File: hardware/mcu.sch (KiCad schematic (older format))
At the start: 43 parts, among them P2 CONN_02X05, SW2 SW_PUSH, U11 TM4C1294KCPDT, Y1 NX5032GA

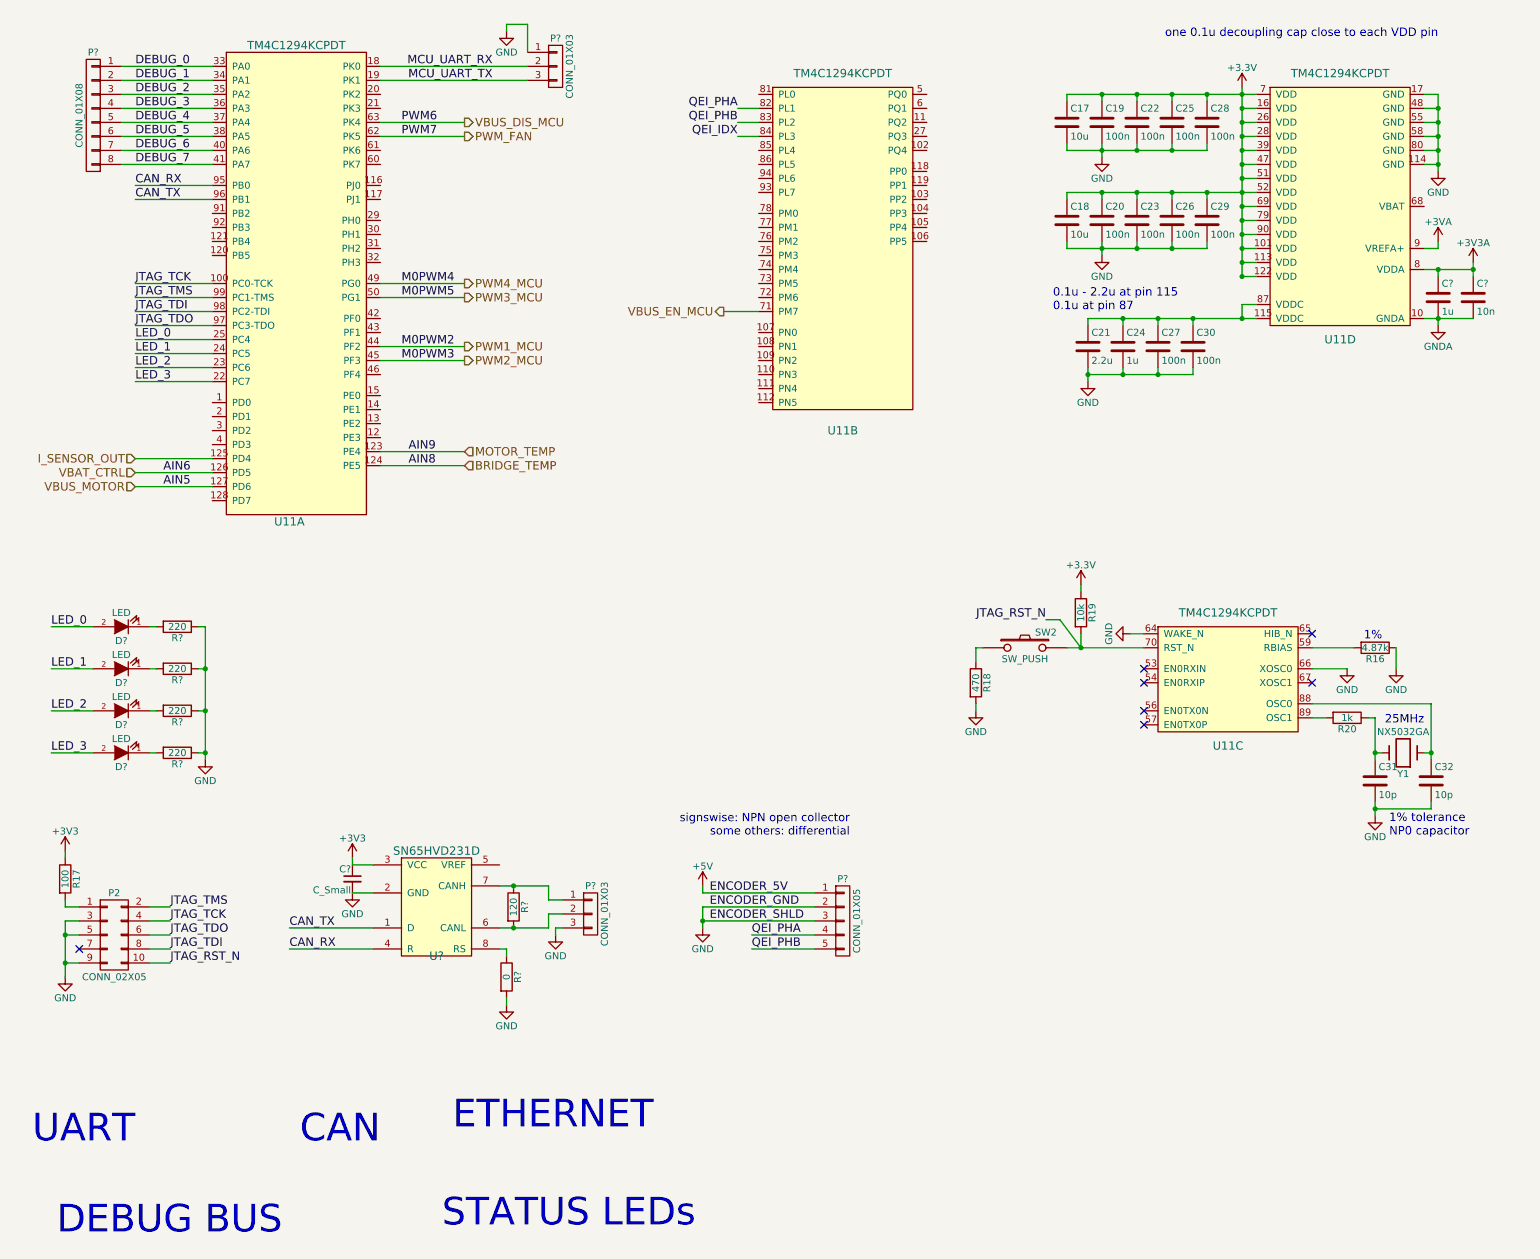
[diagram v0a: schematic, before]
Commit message: Update sensors, hbridge caps, add heatsink
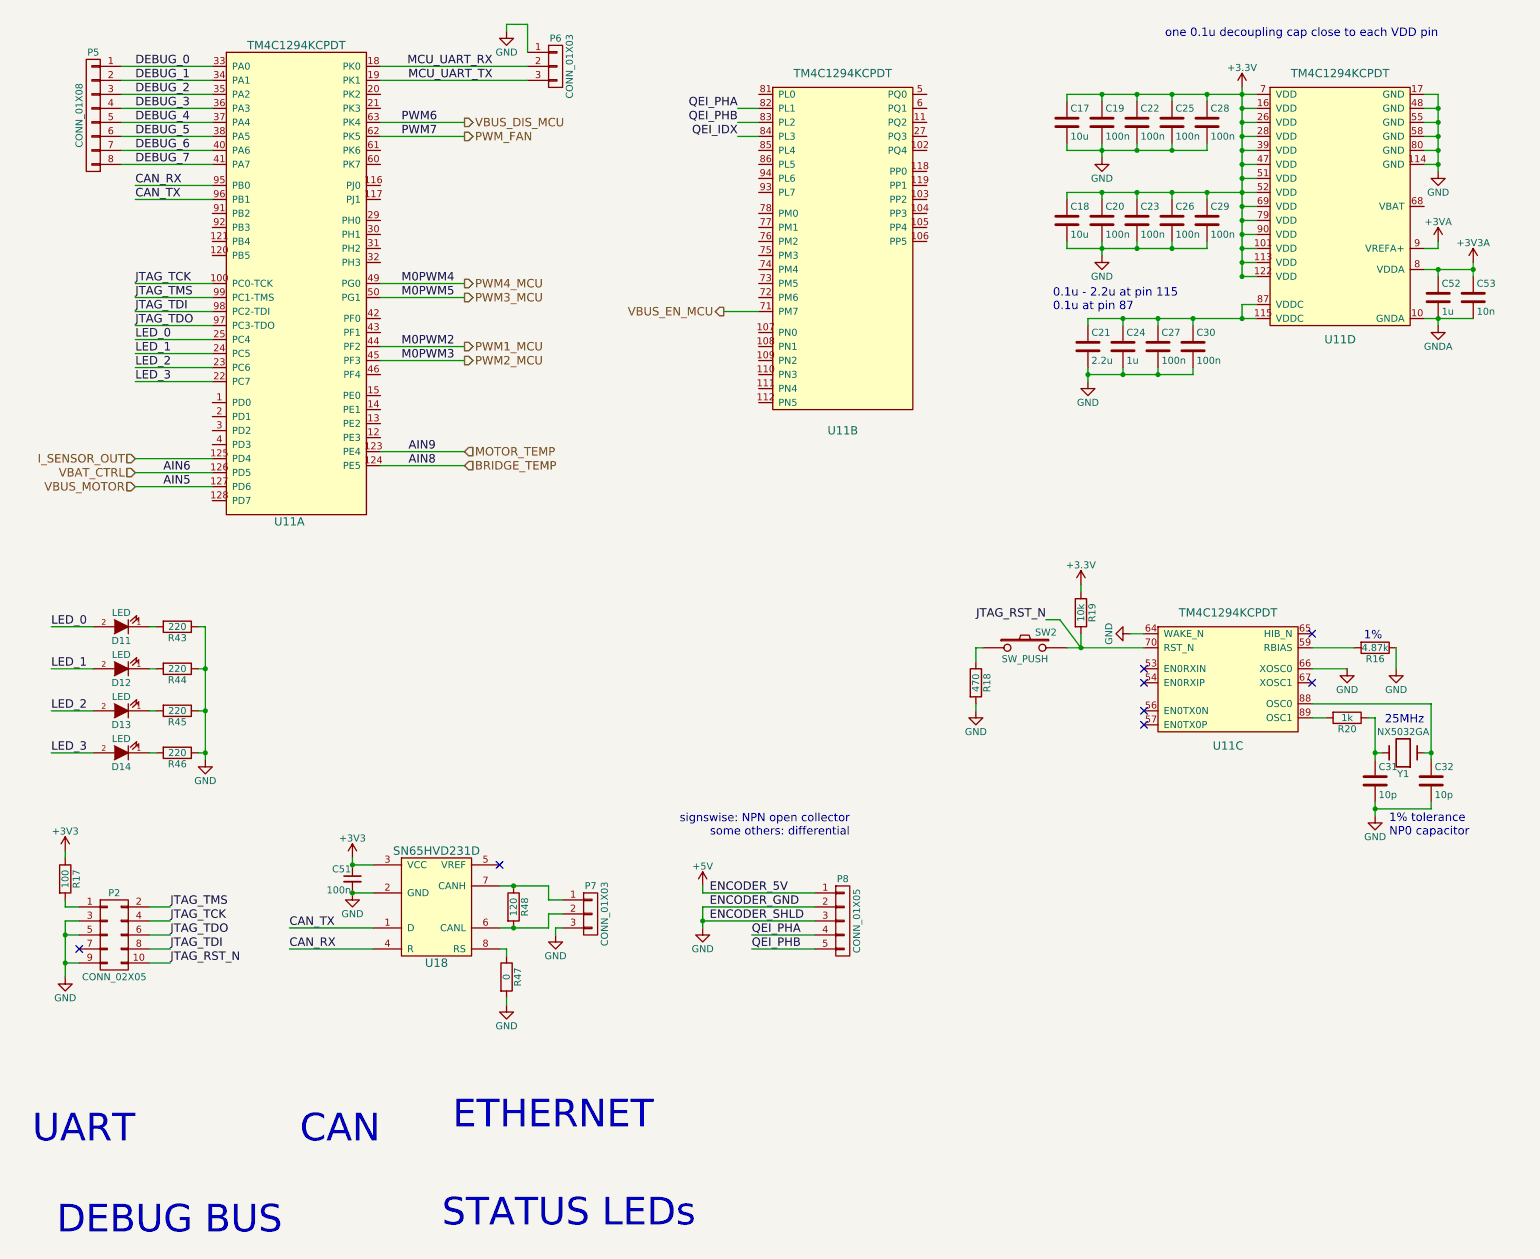
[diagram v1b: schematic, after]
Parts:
- C51: renamed from C?; value C_Small -> 100n
- C52, C53: renamed from C?; footprint (none) -> Capacitors_SMD:C_0603
- gave numbers to parts that had none: 15
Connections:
- no-connect marks 7 -> 8

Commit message: Layout first draft
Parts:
- added JP1, JP2: Jumper_NO_Small, Pin_Headers:Pin_Header_Straight_1x02, symbol Jumper_NO_Small
- C51: footprint (none) -> Capacitors_SMD:C_0603
- U18: footprint (none) -> Housings_SOIC:SOIC-8_3.9x4.9mm_Pitch1.27mm
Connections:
- net GND: now also JP1.1, JP2.1
- net VBUS_ST_MCU: now reaches U11.72 (PM6)
- net CAN_ID_1: now reaches U11.77 (PM1)
- net CAN_ID_1: now also JP2.2
- net CAN_ID_0: now reaches U11.78 (PM0)
- net CAN_ID_0: now also JP1.2
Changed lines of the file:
@@
 F 0 "U18" H 3450 6450 60  0000 C CNN
 F 1 "SN65HVD231D" H 3450 7250 60  0000 C CNN
-F 2 "" H 3400 6850 60  0001 C CNN
+F 2 "Housings_SOIC:SOIC-8_3.9x4.9mm_Pitch1.27mm" H 3400 6850 60  0001 C CNN
 F 3 "" H 3400 6850 60  0000 C CNN
 	1    3450 6850
@@
 F 0 "C51" H 2860 6720 50  0000 L CNN
 F 1 "100n" H 2860 6570 50  0000 L CNN
-F 2 "" H 2850 6650 50  0001 C CNN
+F 2 "Capacitors_SMD:C_0603" H 2850 6650 50  0001 C CNN
 F 3 "" H 2850 6650 50  0000 C CNN
 	1    2850 6650
@@
 Connection ~ 2850 6750
 Connection ~ 2850 6550
+$Comp
+L Jumper_NO_Small JP1
+U 1 1 59B91790
+P 5150 1900
+F 0 "JP1" H 5150 1980 50  0000 C CNN
+F 1 "Jumper_NO_Small" H 5160 1840 50  0001 C CNN
+F 2 "Pin_Headers:Pin_Header_Straight_1x02" H 5150 1900 50  0001 C CNN
+F 3 "" H 5150 1900 50  0000 C CNN
+	1    5150 1900
+	1    0    0    -1
+$EndComp
+$Comp
+L Jumper_NO_Small JP2
+U 1 1 59B93067
+P 5150 2000
+F 0 "JP2" H 5150 2080 50  0000 C CNN
+F 1 "Jumper_NO_Small" H 5160 1940 50  0001 C CNN
+F 2 "Pin_Headers:Pin_Header_Straight_1x02" H 5150 2000 50  0001 C CNN
+F 3 "" H 5150 2000 50  0000 C CNN
+	1    5150 2000
+	1    0    0    -1
+$EndComp
+Wire Wire Line
+	5250 1900 5750 1900
+Wire Wire Line
+	5750 2000 5250 2000
+Wire Wire Line
+	5050 1900 5000 1900
+Wire Wire Line
+	5050 2000 5000 2000
+Wire Wire Line
+	5000 1900 5000 2050
+Connection ~ 5000 2000
+$Comp
+L GND #PWR075
+U 1 1 59B94400
+P 5000 2050
+F 0 "#PWR075" H 5000 1800 50  0001 C CNN
+F 1 "GND" H 5000 1900 50  0000 C CNN
+F 2 "" H 5000 2050 50  0000 C CNN
+F 3 "" H 5000 2050 50  0000 C CNN
+	1    5000 2050
+	1    0    0    -1
+$EndComp
+Text Label 5300 1900 0    60   ~ 0
+CAN_ID_0
+Text Label 5300 2000 0    60   ~ 0
+CAN_ID_1
+Text HLabel 5500 2500 0    60   Output ~ 0
+VBUS_ST_MCU
+Wire Wire Line
+	5500 2500 5750 2500
 $EndSCHEMATC

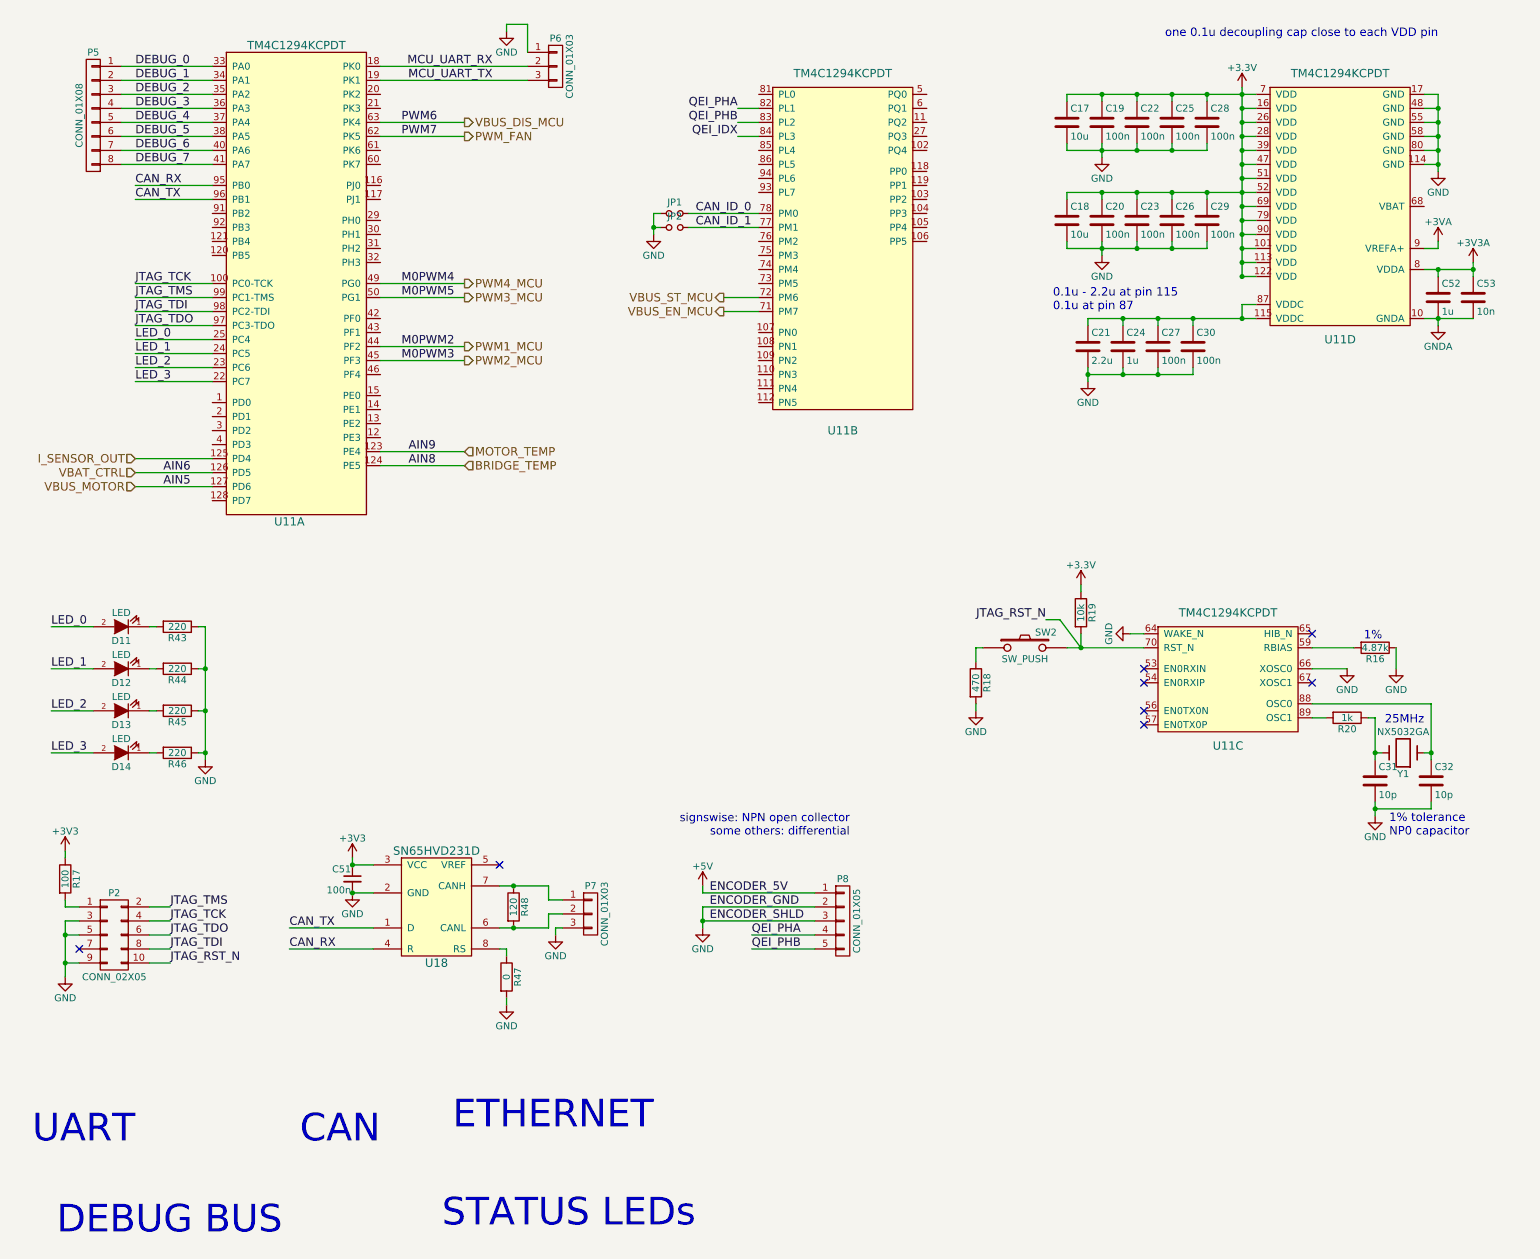
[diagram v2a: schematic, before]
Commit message: Added most footprints, did non-power layout
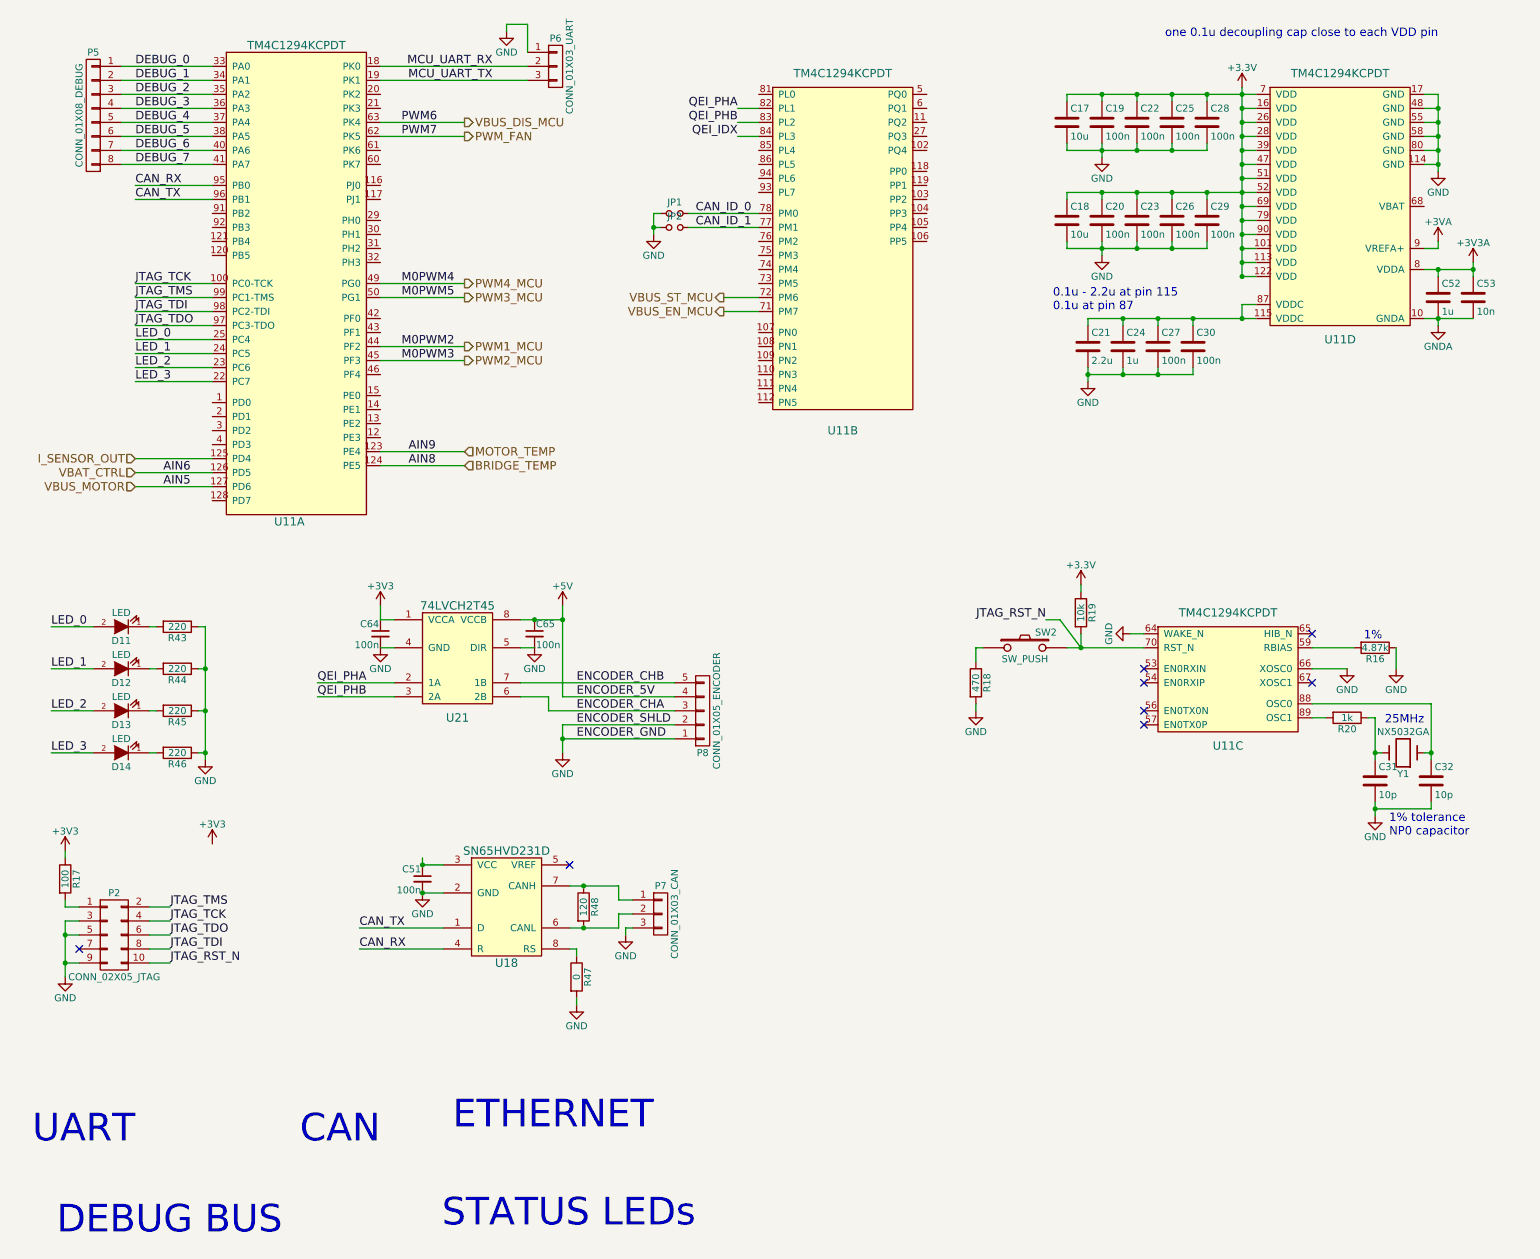
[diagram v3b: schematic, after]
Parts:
- added C64, C65: 100n, Capacitors_SMD:C_0603, symbol C_Small
- added U21: 74LVCH2T45, 2kwMotorController:VSSOP8, symbol 74LVCH2T45
- P2: value CONN_02X05 -> CONN_02X05_JTAG; footprint (none) -> Pin_Headers:Pin_Header_Straight_2x05_Pitch1.27mm
- P5: value CONN_01X08 -> CONN_01X08_DEBUG; footprint (none) -> Pin_Headers:Pin_Header_Straight_1x08
- P6: value CONN_01X03 -> CONN_01X03_UART; footprint (none) -> 2kwMotorController:TERM_3P_2-5_1990012
- P7: value CONN_01X03 -> CONN_01X03_CAN; footprint (none) -> 2kwMotorController:TERM_3P_2-5_1990012
- P8: value CONN_01X05 -> CONN_01X05_ENCODER; footprint (none) -> 2kwMotorController:TERM_5P_2-5_1990038
- R43, R44, R45, R46, R47, R48: footprint (none) -> Resistors_SMD:R_0603
- SW2: footprint (none) -> Buttons_Switches_ThroughHole:SW_PUSH_SMALL
- U11: footprint Housings_QFP:TQFP-128_14x14mm_Pitch0.4mm -> 2kwMotorController:TQFP-128_14x14mm_Pitch0.4mm_LONG
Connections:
- net +3V3: now also C64.1, U21.1 (VCCA); no longer C51.1, U18.3 (VCC)
- net +5V: now also P8.4 (P4), C65.1, U21.8 (VCCB); no longer P8.1 (P1)
- net GND: now also P8.1 (P1), C64.2, C65.2, U21.4 (GND), U21.5 (DIR); no longer P8.3 (P3)
- net QEI_PHA: now also U21.2 (1A); no longer P8.4 (P4)
- net QEI_PHB: now also U21.3 (2A); no longer P8.5 (P5)
- new net: C51.1, U18.3 (VCC)
- new net ENCODER_CHA: P8.3 (P3), U21.6 (2B)
- new net ENCODER_CHB: P8.5 (P5), U21.7 (1B)
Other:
- note removed: "signswise: NPN open collector\nsome others: differential"
- moved on the sheet: C51, P7, P8, R47, R48, U18
